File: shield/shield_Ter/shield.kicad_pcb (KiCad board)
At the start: 2 copper layers, 22 parts, among them CN10 Conn_02x17_Odd_Even, CN7 Conn_02x10_Odd_Even, CN8 Conn_02x08_Odd_Even, CN9 Conn_02x15_Odd_Even, J1 Screw_Terminal_01x04, J10 Screw_Terminal_01x04, J11 Screw_Terminal_01x02, J2 Screw_Terminal_01x04, J3 Screw_Terminal_01x04, J4 Screw_Terminal_01x04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

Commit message: PCB with Aquario con
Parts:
- removed J10: Screw_Terminal_01x04, Buchanan:TE_284513-4
- removed J11: Screw_Terminal_01x02, Buchanan:TE_284513-4
- added H1: MountingHole, MountingHole:MountingHole_3.5mm, F.Cu at (146.1, 181.6)
- added H2: MountingHole, MountingHole:MountingHole_3.5mm, F.Cu at (146.1, 48.3)
- added H3: MountingHole, MountingHole:MountingHole_3.5mm, F.Cu at (66.0, 181.6)
- added H4: MountingHole, MountingHole:MountingHole_3.5mm, F.Cu at (66.0, 48.3)
- J1, J2, J3, J4, J5: value Screw_Terminal_01x04 -> Screw_Terminal_01x05; footprint Buchanan:TE_284513-4 -> TerminalBlock_Phoenix:TerminalBlock_Phoenix_MKDS-1,5-5-5.08_1x05_P5.08mm_Horizontal
- J6, J7, J8, J9: footprint Buchanan:TE_284513-4 -> TerminalBlock_Phoenix:TerminalBlock_Phoenix_MKDS-1,5-5-5.08_1x05_P5.08mm_Horizontal
- moved J5 122.7 mm to (48.3, 157.5)
- moved J9 117.7 mm to (160.0, 174.0)
- moved J8 115.2 mm to (160.0, 147.3)
- moved J4 109.8 mm to (48.3, 130.8)
- moved J7 54.7 mm to (160.0, 120.7), turned to 90 degrees
- moved J1 50.8 mm to (48.3, 50.8), turned to 270 degrees
- moved J3 38.1 mm to (48.3, 104.1), turned to 270 degrees
- moved C_RFID1 12.7 mm to (162.6, 67.3)
- moved J6 10.5 mm to (160.0, 94.0), turned to 90 degrees
- moved C_SOBST1 9.59 mm to (57.1, 50.8)
- moved C_SLINHA1 6.48 mm to (57.1, 71.1), turned to 270 degrees
- moved J2 6.35 mm to (48.3, 77.5), turned to 270 degrees
- moved C_BLUE1 2.54 mm to (102.9, 188.0)
- moved PS_3V3 2.54 mm to (96.5, 27.9)
- moved Bluetooth1 1.91 mm to (113.0, 193.0)
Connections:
- J1 pad 1: PA7 -> +5V
- J1 pad 2: PF10 -> GND
- J1 pad 3: PF5 -> PA3
- J1 pad 4: PF3 -> GND
- J2 pad 1: PC3 -> +3V3
- J2 pad 3: +3V3 -> PC3
- J2 pad 4: +3V3 -> PF3
- J3 pad 1: GND -> PF10
- J3 pad 2: PA3 -> PA7
- J3 pad 3: GND -> PF2
- J3 pad 4: +5V -> PE5
- J4 pad 1: PA6 -> PE6
- J4 pad 2: PD14 -> PF0
- J4 pad 3: PD15 -> PE3
- J5 pad 1: PD2 -> PD0
- J5 pad 2: PB8 -> PF7
- J5 pad 3: PB9 -> PD1
- J5 pad 4: PA5 -> PF9
- J6 pad 2: PC10 -> GND
- J6 pad 3: PC11 -> +3V3
- J6 pad 4: PC12 -> PC8
- J7 pad 1: GND -> PB8
- J7 pad 2: PC8 -> PD2
- J7 pad 3: +3V3 -> PC12
- J7 pad 4: GND -> PC11
- J8 pad 1: PE6 -> PD15
- J8 pad 2: PF1 -> PD14
- J8 pad 3: PE5 -> PA6
- J8 pad 4: PF2 -> PA5
- J9 pad 1: PF8 -> PE15
- J9 pad 2: GND -> PE14
- J9 pad 3: PE3 -> PE12
- J9 pad 4: PF0 -> PE10
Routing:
- net GND: track 68.6 -> 0.00 mm
- net PG0: track 49.7 -> 0.00 mm
- net PE15: track 0.00 -> 45.4 mm
- net PE12: track 0.00 -> 43.8 mm
- net PE14: track 0.00 -> 43.6 mm
- net PE10: track 0.00 -> 41.5 mm
- net PB9: track 37.6 -> 65.5 mm
- net PD15: track 38.3 -> 65.8 mm
- net PA6: track 38.3 -> 64.7 mm
- net PD14: track 37.1 -> 63.3 mm
- net PA5: track 36.0 -> 62.2 mm
- net PD2: track 102.5 -> 127.3 mm
- net PB8: track 37.1 -> 61.7 mm
- net PC12: track 99.1 -> 122.2 mm
- net PC11: track 97.5 -> 119.4 mm
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
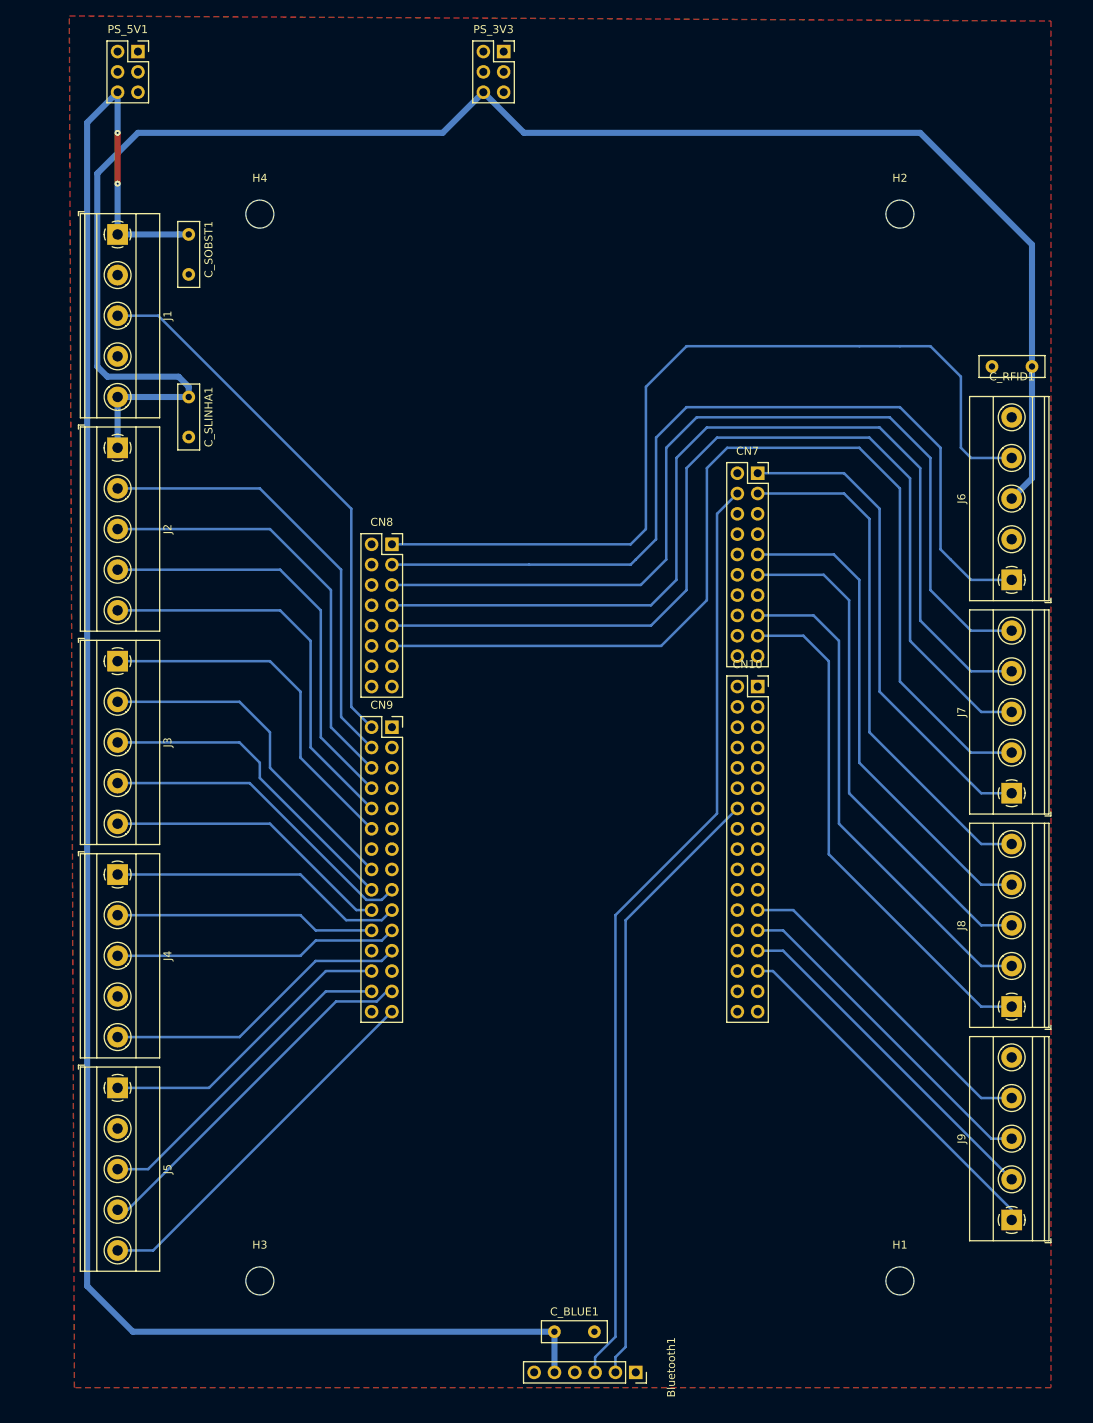
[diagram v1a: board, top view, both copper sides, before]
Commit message: Corrected PCB
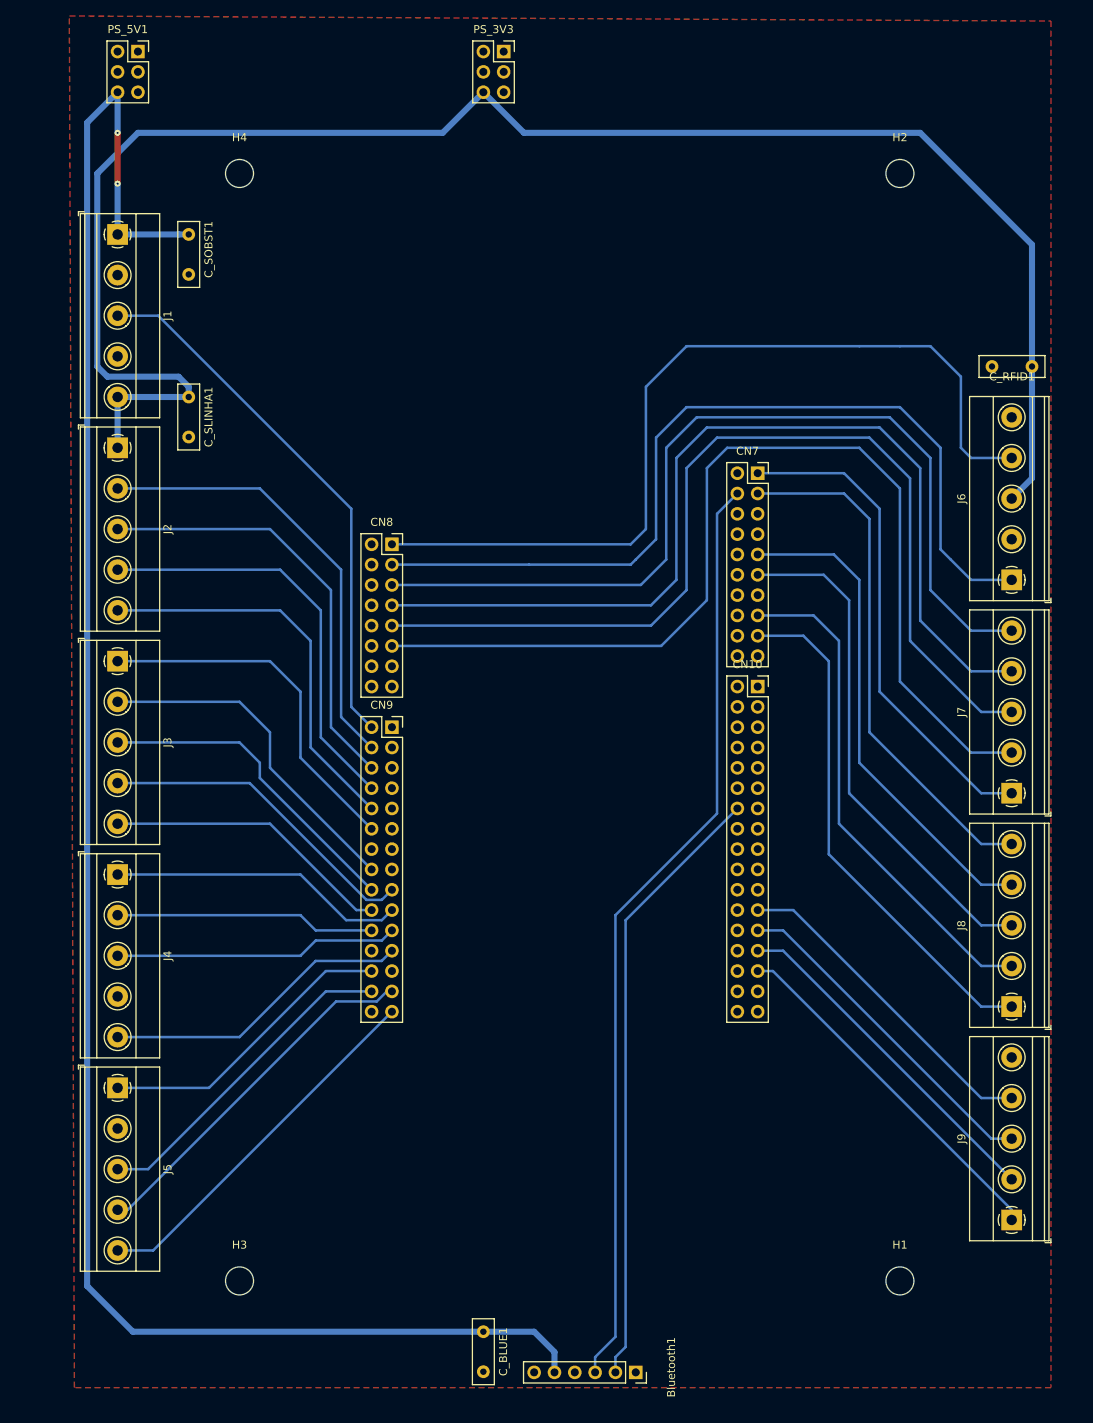
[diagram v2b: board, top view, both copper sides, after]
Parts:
- moved C_BLUE1 8.88 mm to (94.0, 188.0), turned to 270 degrees
- moved H4 5.68 mm to (63.5, 43.2)
- moved H2 5.08 mm to (146.1, 43.2)
- moved H3 2.54 mm to (63.5, 181.6)
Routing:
- net +5V: track 244.0 -> 242.5 mm
